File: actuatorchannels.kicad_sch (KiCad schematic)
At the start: 102 parts

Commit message: more notes, generate pdf
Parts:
- gave numbers to parts that had none: 102
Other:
- note added: "I2C address is 0100 A2 A1 A0 Channels 1-8 at 0x20 Channels 9-16 at 0x21"
- note added: "LED on when channel is on"
- note added: "SSRs rated for 2A output, trigger with 5-25mA Forward voltage of internal LED is 1.1-1.4V 270Ω limits input current to 12.2mA max 8 channels: 16A output, 98mA input 16 channels: 32A output, 196mA input Falstad circuit sim with LED forward voltage: 8-9mA per"
- note added: "Set ACT_CH3 low to actuate solenoid HIGH state is minimum 2.9V Max sink: 250mA total, 25mA per pin Max source: 160mA total, 10mA per pin All channels on: 96mA sink by PCA9534 All channels off: 0-12mA sink by PCA9534"

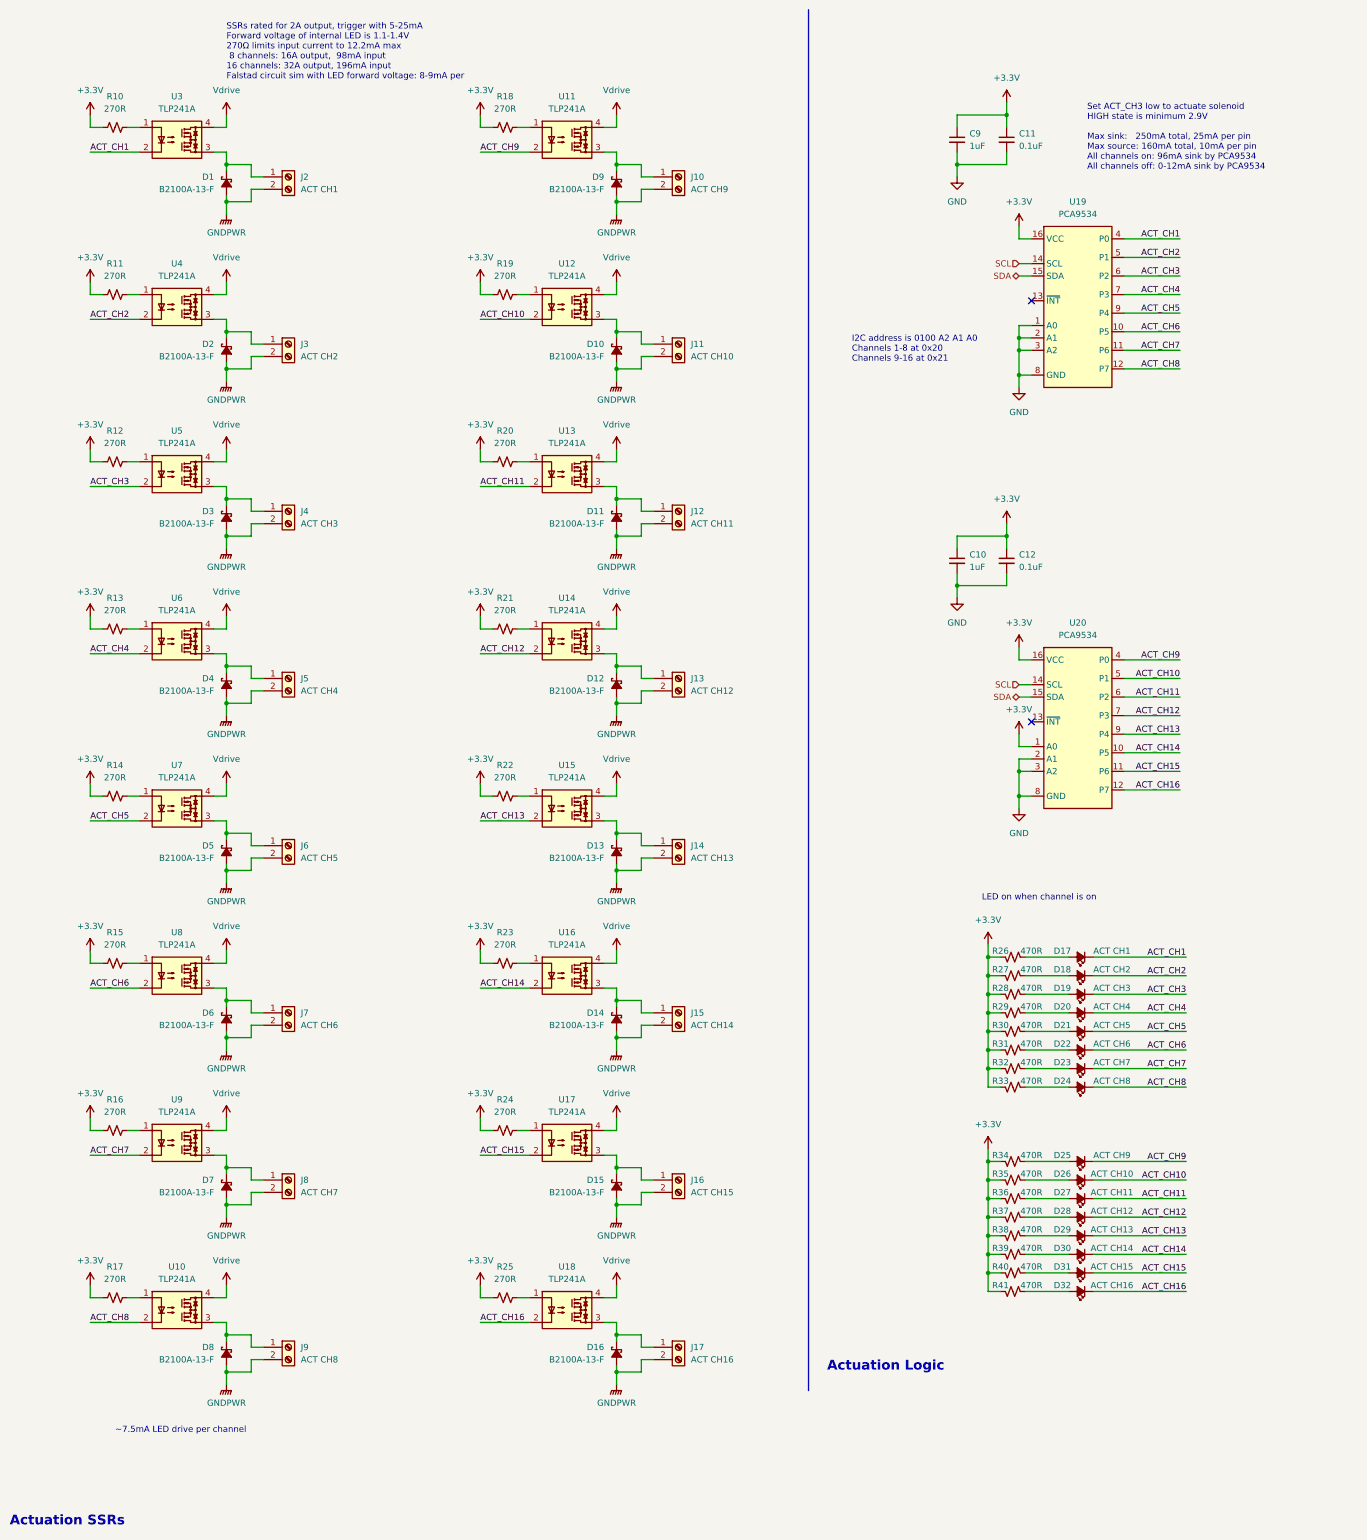
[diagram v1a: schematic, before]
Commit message: estimate 3.3V current consumption
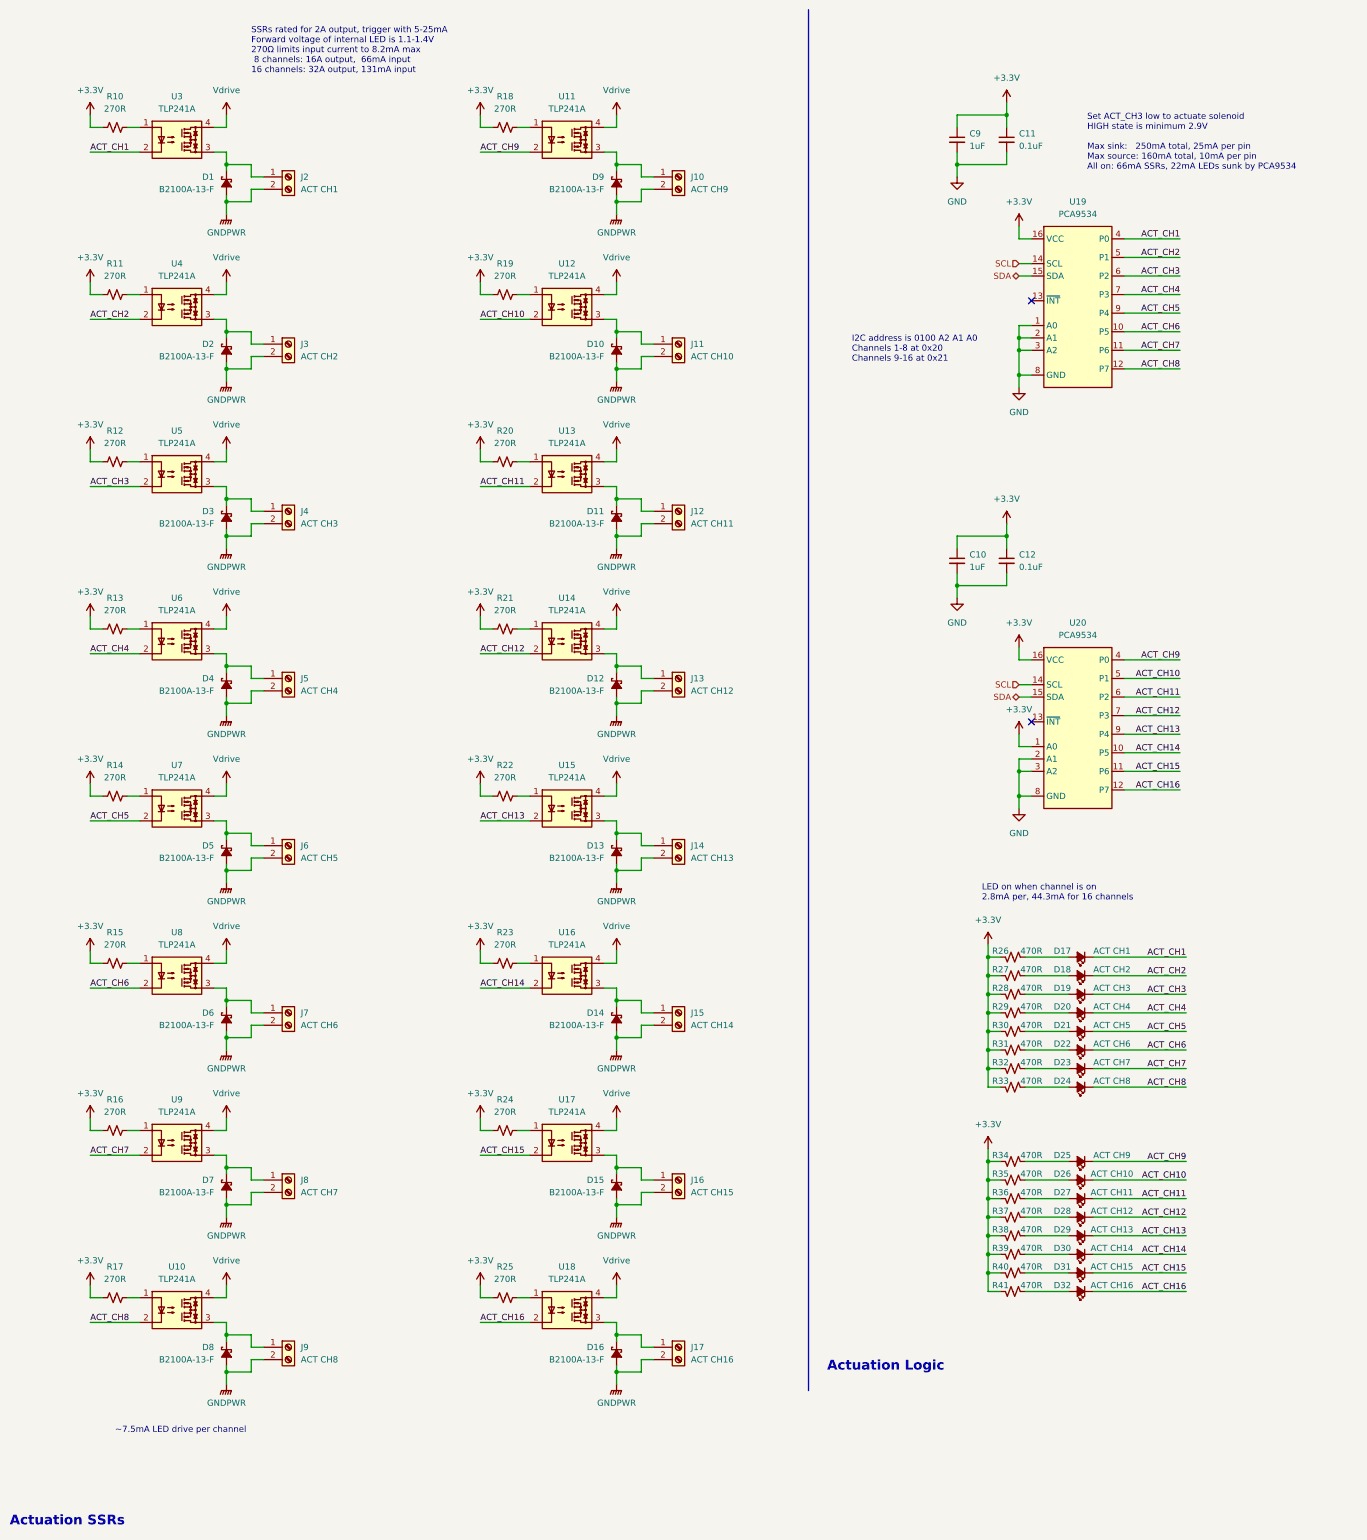
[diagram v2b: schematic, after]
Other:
- note added: "LED on when channel is on 2.8mA per, 44.3mA for 16 channels"
- note added: "SSRs rated for 2A output, trigger with 5-25mA Forward voltage of internal LED is 1.1-1.4V 270Ω limits input current to 8.2mA max 8 channels: 16A output, 66mA input 16 channels: 32A output, 131mA input"
- note added: "Set ACT_CH3 low to actuate solenoid HIGH state is minimum 2.9V Max sink: 250mA total, 25mA per pin Max source: 160mA total, 10mA per pin All on: 66mA SSRs, 22mA LEDs sunk by PCA9534"
- note removed: "LED on when channel is on"
- note removed: "SSRs rated for 2A output, trigger with 5-25mA Forward voltage of internal LED is 1.1-1.4V 270Ω limits input current to 12.2mA max 8 channels: 16A output, 98mA input 16 channels: 32A output, 196mA input Falstad circuit sim with LED forward voltage: 8-9mA per"
- note removed: "Set ACT_CH3 low to actuate solenoid HIGH state is minimum 2.9V Max sink: 250mA total, 25mA per pin Max source: 160mA total, 10mA per pin All channels on: 96mA sink by PCA9534 All channels off: 0-12mA sink by PCA9534"

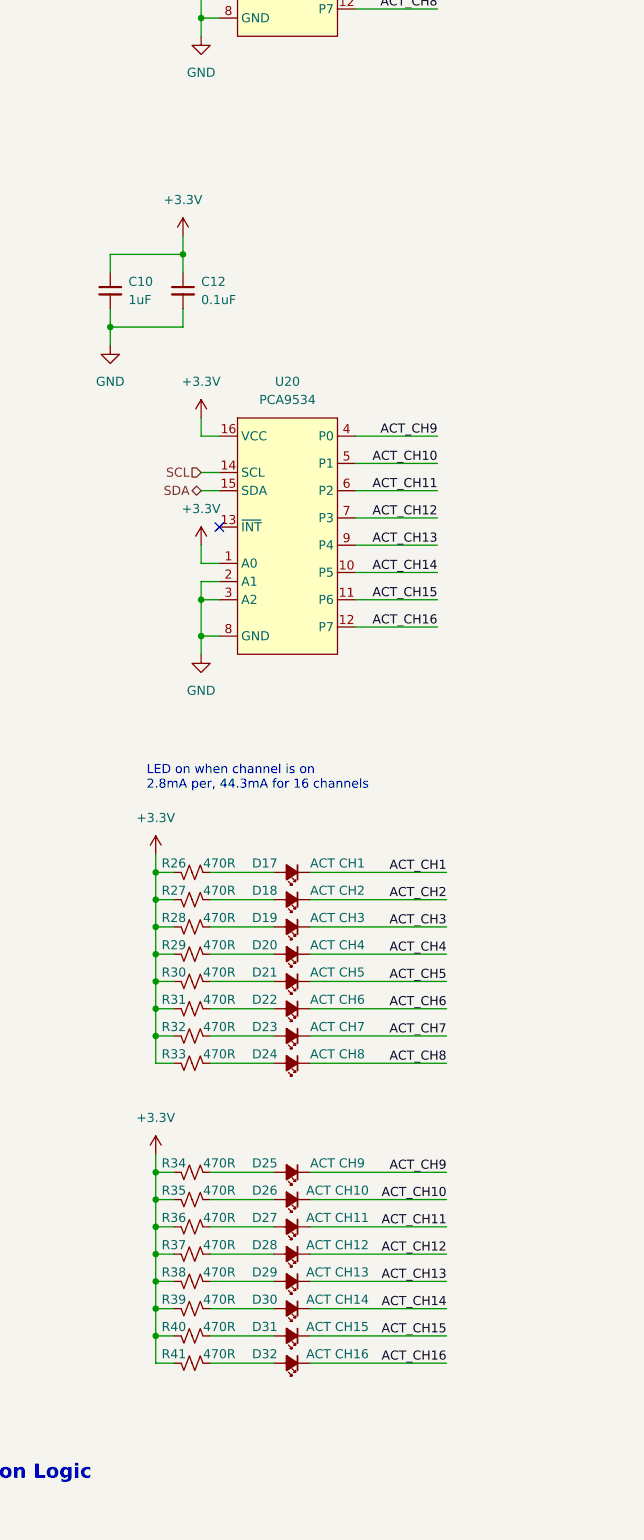
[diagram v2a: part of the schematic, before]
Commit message: labeled chips with their function
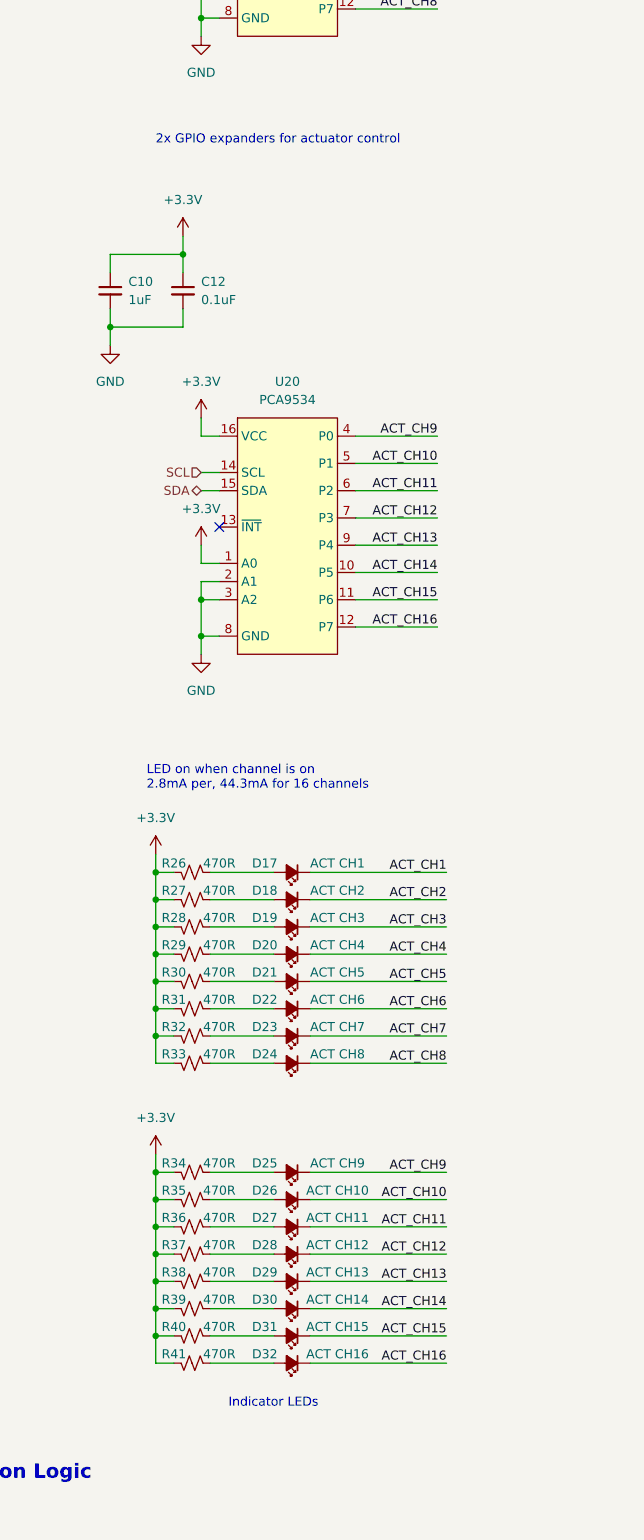
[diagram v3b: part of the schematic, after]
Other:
- note added: "2x GPIO expanders for actuator control"
- note added: "Indicator LEDs"
